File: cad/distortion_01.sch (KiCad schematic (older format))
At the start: 100 parts, among them CON101 Ext_PSU, J101 JACK_IN, J102 JACK_OUT, P101 Battery_conn, P102 BYPASS_SWITCH, P103 CONN_01X03, P104 CONN_01X03, P105 CONN_01X03, P106 CONN_01X03, Q101 BS170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

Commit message: Started placement. Output OPA TL074 changed to 2x TL072.
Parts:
- removed U106: TL074, SMD_Packages:SOIC-14_N, symbol TL074
- added C123: 100n, Capacitors_SMD:C_0603_HandSoldering, symbol C_Small
- added U106, U108: TL072, SMD_Packages:SOIC-8-N, symbol TL072
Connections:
- wire segments 300 -> 302

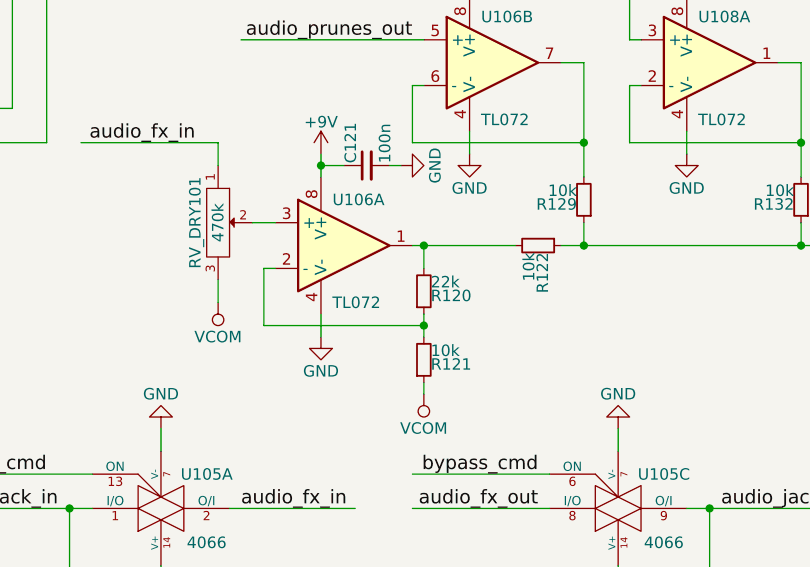
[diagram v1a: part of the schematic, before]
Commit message: Added 220p capa in feedback loop of dry OPA. Placed all components on PCB.
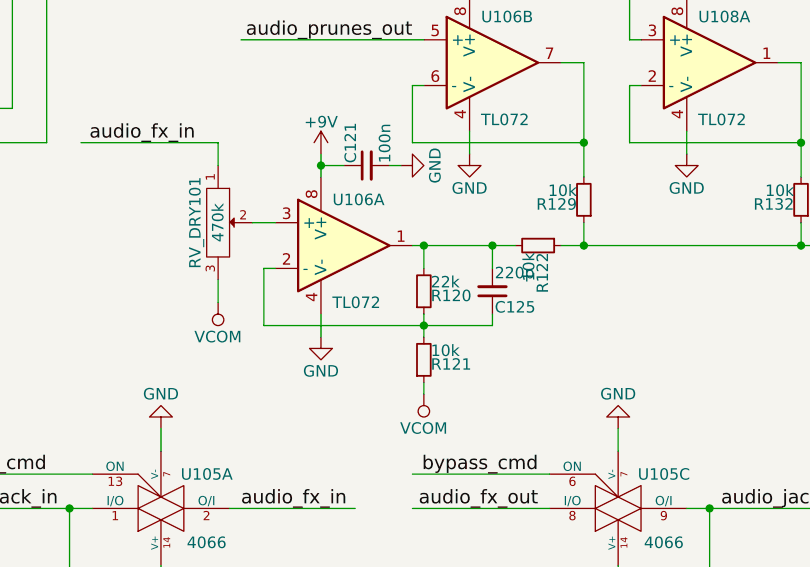
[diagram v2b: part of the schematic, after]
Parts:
- added C125: 220p, Capacitors_SMD:C_0603_HandSoldering, symbol C_Small
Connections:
- wire segments 302 -> 304
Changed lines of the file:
@@
 	7400 4100 7400 4350
 Wire Wire Line
-	7400 4350 8100 4350
+	7400 4350 8400 4350
 Connection ~ 8100 4350
 $Comp
@@
 Wire Wire Line
 	9350 2850 9250 2850
+$Comp
+L C_Small C125
+U 1 1 58BAB592
+P 8400 4200
+F 0 "C125" H 8410 4270 50  0000 L CNN
+F 1 "220p" H 8410 4120 50  0000 L CNN
+F 2 "Capacitors_SMD:C_0603_HandSoldering" H 8400 4200 50  0001 C CNN
+F 3 "" H 8400 4200 50  0000 C CNN
+	1    8400 4200
+	1    0    0    1
+$EndComp
+Wire Wire Line
+	8400 4100 8400 4000
+Connection ~ 8400 4000
+Wire Wire Line
+	8400 4350 8400 4300
 $EndSCHEMATC

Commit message: Finished layout.
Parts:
- RV_DRY101, RV_GAIN101, RV_OCD101, RV_PRUNES101: symbol POT -> POT-RESCUE-distortion_01
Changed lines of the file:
@@
 EESchema Schematic File Version 2
+LIBS:distortion_01-rescue
 LIBS:power
 LIBS:device
@@
 $EndComp
 $Comp
-L POT RV_GAIN101
+L POT-RESCUE-distortion_01 RV_GAIN101
 U 1 1 58A04F01
 P 1500 3750
@@
 $EndComp
 $Comp
-L POT RV_OCD101
+L POT-RESCUE-distortion_01 RV_OCD101
 U 1 1 58A07CE8
 P 4800 3550
@@
 audio_prunes_out
 $Comp
-L POT RV_PRUNES101
+L POT-RESCUE-distortion_01 RV_PRUNES101
 U 1 1 58A161C1
 P 10900 1450
@@
 audio_fx_out
 $Comp
-L POT RV_DRY101
+L POT-RESCUE-distortion_01 RV_DRY101
 U 1 1 58A249E3
 P 7200 3900

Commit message: Continued layout
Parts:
- RV_DRY101, RV_GAIN101, RV_OCD101, RV_PRUNES101: footprint flax_lib:alpha_rv141F -> flax_lib:PTV09
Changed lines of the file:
@@
 F 0 "RV_GAIN101" H 1500 3650 50  0000 C CNN
 F 1 "1M" H 1500 3750 50  0000 C CNN
-F 2 "flax_lib:alpha_rv141F" H 1500 3750 50  0001 C CNN
+F 2 "flax_lib:PTV09" H 1500 3750 50  0001 C CNN
 F 3 "" H 1500 3750 50  0000 C CNN
 	1    1500 3750
@@
 F 0 "RV_OCD101" H 4800 3450 50  0000 C CNN
 F 1 "470k" H 4800 3550 50  0000 C CNN
-F 2 "flax_lib:alpha_rv141F" H 4800 3550 50  0001 C CNN
+F 2 "flax_lib:PTV09" H 4800 3550 50  0001 C CNN
 F 3 "" H 4800 3550 50  0000 C CNN
 	1    4800 3550
@@
 F 0 "RV_PRUNES101" H 10900 1350 50  0000 C CNN
 F 1 "470k" H 10900 1450 50  0000 C CNN
-F 2 "flax_lib:alpha_rv141F" H 10900 1450 50  0001 C CNN
+F 2 "flax_lib:PTV09" H 10900 1450 50  0001 C CNN
 F 3 "" H 10900 1450 50  0000 C CNN
 	1    10900 1450
@@
 F 0 "RV_DRY101" H 7200 3800 50  0000 C CNN
 F 1 "470k" H 7200 3900 50  0000 C CNN
-F 2 "flax_lib:alpha_rv141F" H 7200 3900 50  0001 C CNN
+F 2 "flax_lib:PTV09" H 7200 3900 50  0001 C CNN
 F 3 "" H 7200 3900 50  0000 C CNN
 	1    7200 3900

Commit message: Changed PSU connector footprint to 3w HE10, finished layout.
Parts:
- CON101: footprint Connect:JACK_ALIM -> Pin_Headers:Pin_Header_Straight_1x03_Pitch2.54mm
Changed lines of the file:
@@
 F 0 "CON101" H 900 7400 50  0000 C CNN
 F 1 "Ext_PSU" H 900 6950 50  0000 C CNN
-F 2 "Connect:JACK_ALIM" H 900 7150 50  0001 C CNN
+F 2 "Pin_Headers:Pin_Header_Straight_1x03_Pitch2.54mm" H 900 7150 50  0001 C CNN
 F 3 "" H 900 7150 50  0000 C CNN
 	1    900  7150

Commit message: Added LTspice simulation.
Added 10n cap on OCD output.
Added 10u cap on Vref for HF stability.
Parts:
- added C126: 10u, Capacitors_SMD:CP_Elec_5x4.5, symbol CP1_Small
- added C127: 10n, Capacitors_SMD:C_0603_HandSoldering, symbol C_Small
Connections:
- wire segments 304 -> 308
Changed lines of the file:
@@
 LIBS:contrib
 LIBS:valves
-LIBS:flax_lib
 LIBS:distortion_01-cache
 EELAYER 25 0
@@
 	1700 6900 1700 6800
 Wire Wire Line
-	2700 6900 2300 6900
+	2100 6900 2700 6900
 Connection ~ 3400 7000
 Wire Wire Line
@@
 	4600 2800 4600 2900
 Wire Wire Line
-	4800 3200 4600 3200
+	4350 3200 4800 3200
 Connection ~ 4600 3200
 Wire Wire Line
@@
 	0    -1   -1   0
 $EndComp
+$Comp
+L C_Small C127
+U 1 1 59AD31E5
+P 4350 4100
+F 0 "C127" H 4360 4170 50  0000 L CNN
+F 1 "10n" H 4360 4020 50  0000 L CNN
+F 2 "Capacitors_SMD:C_0603_HandSoldering" H 4350 4100 50  0001 C CNN
+F 3 "" H 4350 4100 50  0001 C CNN
+	1    4350 4100
+	1    0    0    -1
+$EndComp
+$Comp
+L VCOM #PWR078
+U 1 1 59AD34C7
+P 4350 4300
+F 0 "#PWR078" H 4350 4150 50  0001 C CNN
+F 1 "VCOM" H 4350 4450 50  0000 C CNN
+F 2 "" H 4350 4300 50  0000 C CNN
+F 3 "" H 4350 4300 50  0000 C CNN
+	1    4350 4300
+	-1   0    0    1
+$EndComp
+Wire Wire Line
+	4350 4000 4350 3200
+Wire Wire Line
+	4350 4200 4350 4300
+$Comp
+L CP1_Small C126
+U 1 1 59AD3D80
+P 2100 7100
+F 0 "C126" H 2110 7170 50  0000 L CNN
+F 1 "10u" H 2110 7020 50  0000 L CNN
+F 2 "Capacitors_SMD:CP_Elec_5x4.5" H 2100 7100 50  0001 C CNN
+F 3 "" H 2100 7100 50  0000 C CNN
+	1    2100 7100
+	1    0    0    -1
+$EndComp
+Wire Wire Line
+	2100 7000 2100 6900
+$Comp
+L GND #PWR079
+U 1 1 59AD40DD
+P 2100 7300
+F 0 "#PWR079" H 2100 7050 50  0001 C CNN
+F 1 "GND" H 2100 7150 50  0000 C CNN
+F 2 "" H 2100 7300 50  0000 C CNN
+F 3 "" H 2100 7300 50  0000 C CNN
+	1    2100 7300
+	1    0    0    -1
+$EndComp
+Wire Wire Line
+	2100 7200 2100 7300
 $EndSCHEMATC
